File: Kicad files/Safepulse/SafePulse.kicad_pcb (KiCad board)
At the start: 4 copper layers, 40.6 x 20.8 mm, 90 parts, among them J1 Conn_01x03_Male, Q1 FQT7N10L, Q2 BC846A, Q3 MMBT3906, Q4 MMBT3906, U1 TS4061AILT-1.25, U2 74HC14, U3 TLV27L1DBVT, U33 MAX9910EXK+T, U4 CD14538BM

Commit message: Updated with Gerbers
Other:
- outline, holes or cut-outs redrawn
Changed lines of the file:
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@@
   (gr_line (start 165.52 57.658) (end 137.414 57.658) (layer "F.SilkS") (width 0.15))
   (gr_line (start 165.52 57.658) (end 166.604 58.658) (layer "F.SilkS") (width 0.15))
-  (gr_arc (start 165.347 76.47) (end 166.847 76.47) (angle 90) (layer "Edge.Cuts") (width 0.1))
-  (gr_line (start 165.347 77.97) (end 127.738 77.978) (layer "Edge.Cuts") (width 0.1))
-  (gr_line (start 166.847 58.65) (end 166.847 76.47) (layer "Edge.Cuts") (width 0.1))
-  (gr_arc (start 165.347 58.65) (end 165.347 57.15) (angle 90) (layer "Edge.Cuts") (width 0.1))
-  (gr_rect (start 159.45 68.725) (end 160.65 77.465) (layer "Edge.Cuts") (width 0.1) (fill none))
-  (gr_arc (start 127.738 76.478) (end 127.738 77.978) (angle 90) (layer "Edge.Cuts") (width 0.1))
-  (gr_line (start 127.738 57.158) (end 165.347 57.15) (layer "Edge.Cuts") (width 0.1))
-  (gr_line (start 126.238 76.478) (end 126.238 58.658) (layer "Edge.Cuts") (width 0.1))
-  (gr_arc (start 127.738 58.658) (end 126.238 58.658) (angle 90) (layer "Edge.Cuts") (width 0.1))
+  (gr_arc (start 165.3 76.465) (end 166.8 76.465) (angle 90) (layer "Edge.Cuts") (width 0.1))
+  (gr_line (start 165.3 77.965) (end 127.738 77.965) (layer "Edge.Cuts") (width 0.1))
+  (gr_line (start 166.8 58.665) (end 166.8 76.465) (layer "Edge.Cuts") (width 0.1))
+  (gr_arc (start 127.738 58.665) (end 126.238 58.665) (angle 90) (layer "Edge.Cuts") (width 0.1))
+  (gr_arc (start 165.3 58.665) (end 165.3 57.165) (angle 90) (layer "Edge.Cuts") (width 0.1))
+  (gr_rect (start 159.45 68.925) (end 160.65 77.465) (layer "Edge.Cuts") (width 0.1) (fill none))
+  (gr_line (start 165.3 57.165) (end 127.738 57.165) (layer "Edge.Cuts") (width 0.1))
+  (gr_arc (start 127.738 76.465) (end 126.238 76.465) (angle -90) (layer "Edge.Cuts") (width 0.1))
+  (gr_line (start 126.238 76.465) (end 126.238 58.665) (layer "Edge.Cuts") (width 0.1))
   (gr_text "GND\n" (at 133.925 73.7) (layer "B.SilkS")
     (effects (font (size 0.5 0.5) (thickness 0.1)) (justify mirror))

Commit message: Merge branch 'main' of https://github.com/Safecast/open-hvps into main
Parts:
- added IC1: S-35770E01I-K8T2U, Counters:SOP65P400X80-8N, B.Cu at (141.2, 62.9)
- added J2: 4208, Connector_Qwiic:4208, B.Cu at (163.4, 61.6)
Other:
- board text added: "SAFEPULSE V1.2.3"
- board text removed: "SAFEPULSE V1.2.2"

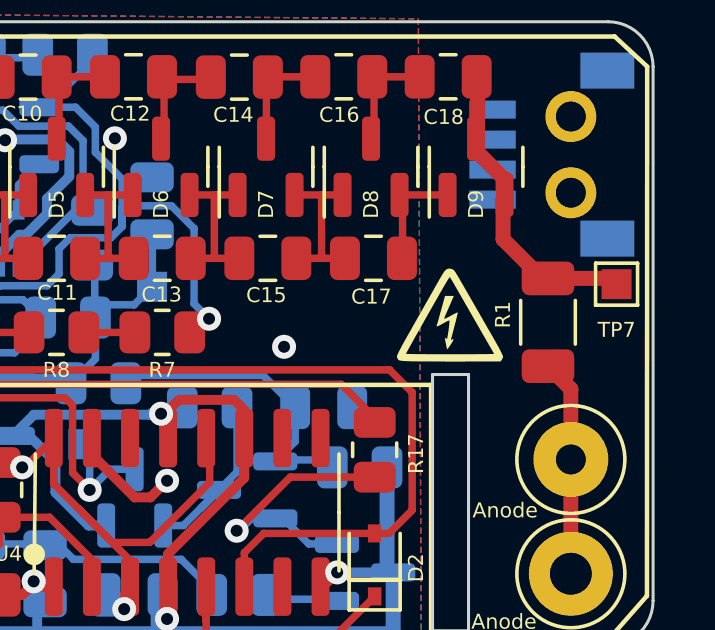
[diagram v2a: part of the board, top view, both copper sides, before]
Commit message: Updated schematic for I2C pulse counting
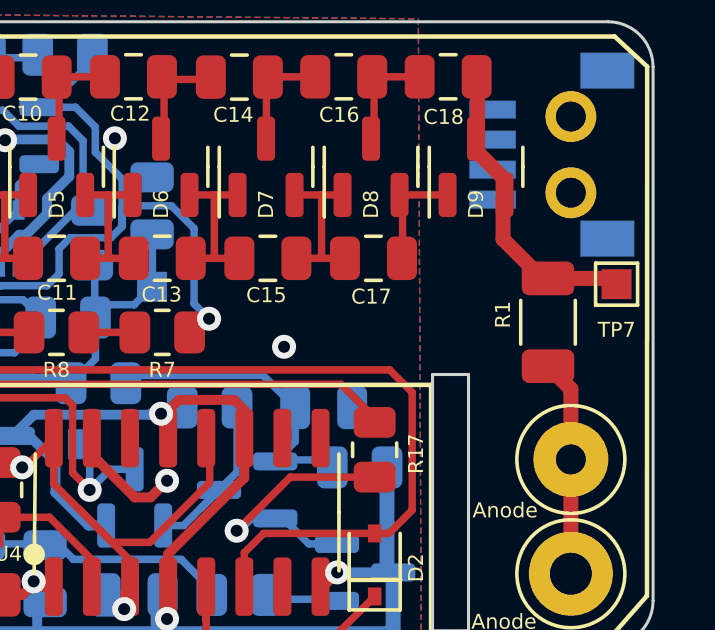
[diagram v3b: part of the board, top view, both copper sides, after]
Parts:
- removed G***: LOGO, Symbol:QR_code_SafePulse
- removed G2, G3: LOGO, Symbol:HV warning
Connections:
- C5 pad 1: Net-(C5-Pad1) -> Net-(D2-Pad2)
- FB2 pad 2: Net-(C5-Pad1) -> Net-(D2-Pad2)
- IC1 pad 3: unconnected-(IC1-Pad3) -> Net-(D2-Pad2)
- J2 pad 2: Net-(IC1-Pad6) -> +3V3
- J2 pad 3: Net-(IC1-Pad7) -> Net-(IC1-Pad6)
- J2 pad 4: +3V3 -> Net-(IC1-Pad7)
- L1 pad 1: Net-(C5-Pad1) -> Net-(D2-Pad2)
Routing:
- net Net-(C5-Pad1): track 6.90 -> 0.00 mm
- net Net-(D2-Pad2): track 43.1 -> 50.0 mm
